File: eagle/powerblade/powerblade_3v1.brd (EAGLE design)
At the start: 27.9 x 27.9 mm, 91 parts, among them J1 JTAG_14PIN_IDC, J21 AC_INTBFILM, J4 TC2030-JLINK-NL, Q1 2N7002, Q3 2SK1829, Q4 2SK1829, U1 TPS62122, U2 MCP6V3, U3 MSP430FR5738, U4 NRF51822QF, U6 MAX9910, U7 OPA2369, X1 16MHz, X2 ABS05-32.768KHZ-9-T, X3 32.768kHz

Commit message: finished parts
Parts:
- R11, R22: value 134k 1% -> 670k
- R12, R13: value 67k 1% -> 330k
- R15: value NP -> 1M 1%
- R16: value 0 -> 75 1%
- R18: value 2.49 1% -> 4.99 1%
- R35: value 2k 1% -> 20k
- R37: value 90k 1% -> 887k 1%
- R38: value 3.1k 1% -> 137k 1%
- R39: value 100k 1% -> 71.5k 1%
- R40: value 100k 1% -> 1M 1%
- R6: value 220k -> 660k
- RF: value 1.5k 1% -> 4.99k 1%
- RI1, RI2: value 220k 1% -> 953k 1%
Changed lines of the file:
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@@
 <attribute name="NAME" x="5.23875" y="-0.762" size="0.762" layer="25" rot="R90"/>
 </element>
-<element name="R15" library="rcl" package="R0402" value="NP" x="3.65125" y="-1.27" smashed="yes">
-<attribute name="DIGIKEY" value="NP" x="3.65125" y="22.86" size="1.778" layer="27" display="off"/>
+<element name="R15" library="rcl" package="R0402" value="1M 1%" x="3.65125" y="-1.27" smashed="yes">
 <attribute name="VALUE" x="2.06375" y="-3.81" size="0.762" layer="27"/>
 </element>
-<element name="R16" library="rcl" package="R0402" value="0" x="3.65125" y="-2.44475" smashed="yes">
-<attribute name="DIGIKEY" value="P0.0JCT-ND" x="-1.42875" y="16.60525" size="1.778" layer="27" display="off"/>
+<element name="R16" library="rcl" package="R0402" value="75 1%" x="3.65125" y="-2.44475" smashed="yes">
 <attribute name="NAME" x="1.42875" y="-4.66725" size="0.762" layer="25"/>
 </element>
@@
 <attribute name="NAME" x="0.4445" y="4.12115" size="0.762" layer="25"/>
 </element>
-<element name="R18" library="rcl" package="R0402" value="2.49 1%" x="3.4925" y="4.28625" smashed="yes" rot="R180">
+<element name="R18" library="rcl" package="R0402" value="4.99 1%" x="3.4925" y="4.28625" smashed="yes" rot="R180">
 <attribute name="DIGIKEY" value="541-2.49LLCT-ND" x="3.4925" y="14.44625" size="1.778" layer="27" rot="R180" display="off"/>
 <attribute name="NAME" x="4.445" y="3.81" size="0.762" layer="25" rot="R180"/>
@@
 <attribute name="NAME" x="-11.39825" y="1.17475" size="0.762" layer="25" rot="R180"/>
 </element>
-<element name="RF" library="rcl" package="R0402" value="1.5k 1%" x="-12.16025" y="7.46125" smashed="yes" rot="R180">
-<attribute name="DIGIKEY" value="P1.50KLCT-ND" x="-4.54025" y="36.67125" size="1.778" layer="27" rot="R180" display="off"/>
+<element name="RF" library="rcl" package="R0402" value="4.99k 1%" x="-12.16025" y="7.46125" smashed="yes" rot="R180">
 <attribute name="NAME" x="-10.8585" y="6.19125" size="0.762" layer="25"/>
 </element>
 <element name="R20" library="rcl" package="R0402" value="1M 1%" x="-12.2555" y="3.14325" smashed="yes" rot="R180">
-<attribute name="DIGIKEY" value="P10.0KLCT-ND" x="10.6045" y="37.43325" size="1.778" layer="27" rot="R180" display="off"/>
 <attribute name="NAME" x="-11.46175" y="0.28575" size="0.762" layer="25" rot="R180"/>
 </element>
 <element name="R21" library="rcl" package="R0402" value="1M 1%" x="-9.11225" y="6.9215" smashed="yes" rot="R270">
-<attribute name="DIGIKEY" value="P10.0KLCT-ND" x="-43.40225" y="6.9215" size="1.778" layer="27" rot="R270" display="off"/>
 <attribute name="NAME" x="-8.47725" y="7.5565" size="0.762" layer="25" rot="R270"/>
 </element>
-<element name="RI1" library="rcl" package="R0402" value="220k 1%" x="-11.58875" y="9.2075" smashed="yes" rot="R270">
-<attribute name="DIGIKEY" value="P220KLCT-ND" x="-61.11875" y="9.2075" size="1.778" layer="27" rot="R270" display="off"/>
+<element name="RI1" library="rcl" package="R0402" value="953k 1%" x="-11.58875" y="9.2075" smashed="yes" rot="R270">
 <attribute name="NAME" x="-10.95375" y="10.63625" size="0.762" layer="25" rot="R270"/>
 </element>
-<element name="RI2" library="rcl" package="R0402" value="220k 1%" x="-9.7155" y="8.5725" smashed="yes" rot="R180">
-<attribute name="DIGIKEY" value="P220KLCT-ND" x="-0.8255" y="63.1825" size="1.778" layer="27" rot="R180" display="off"/>
+<element name="RI2" library="rcl" package="R0402" value="953k 1%" x="-9.7155" y="8.5725" smashed="yes" rot="R180">
 <attribute name="NAME" x="-8.128" y="9.8425" size="0.762" layer="25" rot="R180"/>
 </element>
@@
 <attribute name="NAME" x="-5.36575" y="-5.68325" size="0.762" layer="25" rot="R90"/>
 </element>
-<element name="R35" library="rcl" package="R0402" value="2k 1%" x="-0.635" y="-1.23825" smashed="yes" rot="R90">
+<element name="R35" library="rcl" package="R0402" value="20k" x="-0.635" y="-1.23825" smashed="yes" rot="R90">
 <attribute name="DIGIKEY" value="P2.00KLCT-ND" x="71.755" y="-16.47825" size="1.778" layer="27" rot="R90" display="off"/>
 <attribute name="NAME" x="0.3175" y="-4.572" size="0.762" layer="25" rot="R90"/>
 </element>
-<element name="R37" library="rcl" package="R0402" value="90k 1%" x="-2.8575" y="1.905" smashed="yes" rot="R180">
+<element name="R37" library="rcl" package="R0402" value="887k 1%" x="-2.8575" y="1.905" smashed="yes" rot="R180">
 <attribute name="DIGIKEY" value="P90.9KLCT-ND" x="4.7625" y="79.375" size="1.778" layer="27" rot="R180" display="off"/>
 <attribute name="NAME" x="-1.905" y="1.42875" size="0.762" layer="25" rot="R180"/>
 </element>
-<element name="R38" library="rcl" package="R0402" value="3.1k 1%" x="-2.8575" y="3.048" smashed="yes">
+<element name="R38" library="rcl" package="R0402" value="137k 1%" x="-2.8575" y="3.048" smashed="yes">
 <attribute name="DIGIKEY" value="P3.09KHCT-ND" x="-19.3675" y="-89.662" size="1.778" layer="27" display="off"/>
 <attribute name="NAME" x="-1.27" y="4.318" size="0.762" layer="25"/>
 </element>
-<element name="R40" library="rcl" package="R0402" value="100k 1%" x="-3.96875" y="-2.9845" smashed="yes" rot="R180">
-<attribute name="DIGIKEY" value="P100KLCT-ND" x="11.27125" y="101.1555" size="1.778" layer="27" rot="R180" display="off"/>
+<element name="R40" library="rcl" package="R0402" value="1M 1%" x="-3.96875" y="-2.9845" smashed="yes" rot="R180">
 <attribute name="NAME" x="-3.175" y="-3.77825" size="0.762" layer="25" rot="R180"/>
 </element>
@@
 <attribute name="DIGIKEY" value="5126K-ND" x="158.4325" y="-32.766" size="1.778" layer="27" rot="R90" display="off"/>
 </element>
-<element name="R39" library="rcl" package="R0402" value="100k 1%" x="-1.55575" y="-2.9845" smashed="yes" rot="R180">
+<element name="R39" library="rcl" package="R0402" value="71.5k 1%" x="-1.55575" y="-2.9845" smashed="yes" rot="R180">
 <attribute name="DIGIKEY" value="P100KLCT-ND" x="-1.55575" y="-2.9845" size="1.778" layer="27" rot="R180" display="off"/>
 <attribute name="NAME" x="-0.60325" y="-4.572" size="0.762" layer="25" rot="R180"/>
@@
 <attribute name="DIGIKEY" value="NP" x="-7.62" y="-80.772" size="1.778" layer="27" display="off"/>
 </element>
-<element name="R11" library="rcl" package="R0603" value="134k 1%" x="-6.858" y="-65.532">
-<attribute name="DIGIKEY" value="P133KHCT-ND" x="-15.24" y="-130.302" size="1.778" layer="27" display="off"/>
-</element>
-<element name="R12" library="rcl" package="R0603" value="67k 1%" x="1.524" y="-65.532">
-<attribute name="DIGIKEY" value="P66.5KHCT-ND" x="-15.24" y="-135.636" size="1.778" layer="27" display="off"/>
-</element>
+<element name="R11" library="rcl" package="R0603" value="670k" x="-6.858" y="-65.532"/>
+<element name="R12" library="rcl" package="R0603" value="330k" x="1.524" y="-65.532"/>
 <element name="X3" library="general" package="0805" value="32.768kHz" x="6.858" y="-48.768">
 <attribute name="DIGIKEY" value="535-12373-1-ND" x="-15.24" y="-141.732" size="1.778" layer="27" display="off"/>
@@
 <attribute name="DIGIKEY" value="2SK1829TE85LFCT-ND" x="-12.192" y="-125.73" size="1.778" layer="27" display="off"/>
 </element>
-<element name="R6" library="rcl" package="R0603" value="220k" x="-12.192" y="-129.54"/>
+<element name="R6" library="rcl" package="R0603" value="660k" x="-12.192" y="-129.54"/>
 <element name="R10" library="rcl" package="R0603" value="220k" x="-12.192" y="-134.874"/>
-<element name="R13" library="rcl" package="R0603" value="67k 1%" x="-12.192" y="-140.208">
-<attribute name="DIGIKEY" value="P66.5KHCT-ND" x="-12.192" y="-140.208" size="1.778" layer="27" display="off"/>
-</element>
-<element name="R22" library="rcl" package="R0603" value="134k 1%" x="-12.192" y="-145.542">
-<attribute name="DIGIKEY" value="P133KHCT-ND" x="-12.192" y="-145.542" size="1.778" layer="27" display="off"/>
-</element>
+<element name="R13" library="rcl" package="R0603" value="330k" x="-12.192" y="-140.208"/>
+<element name="R22" library="rcl" package="R0603" value="670k" x="-12.192" y="-145.542"/>
 </elements>
 <signals>

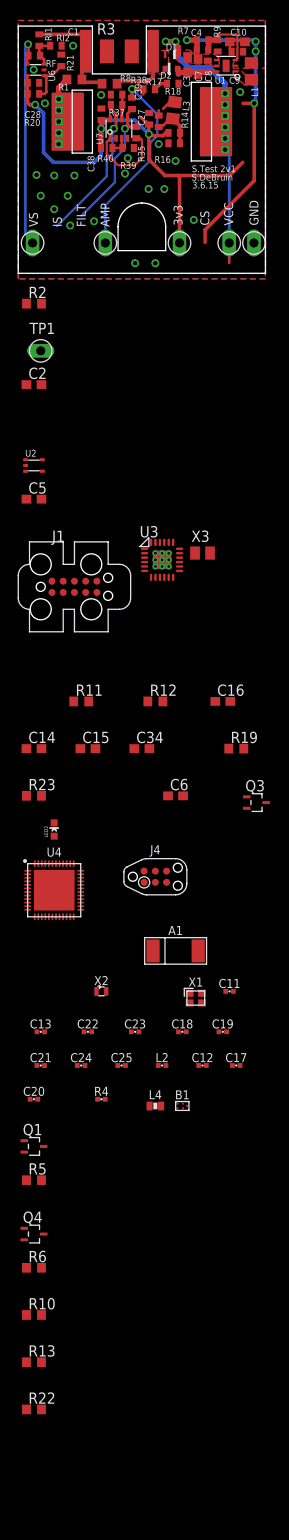
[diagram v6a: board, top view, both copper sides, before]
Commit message: post mortem changes to schematic
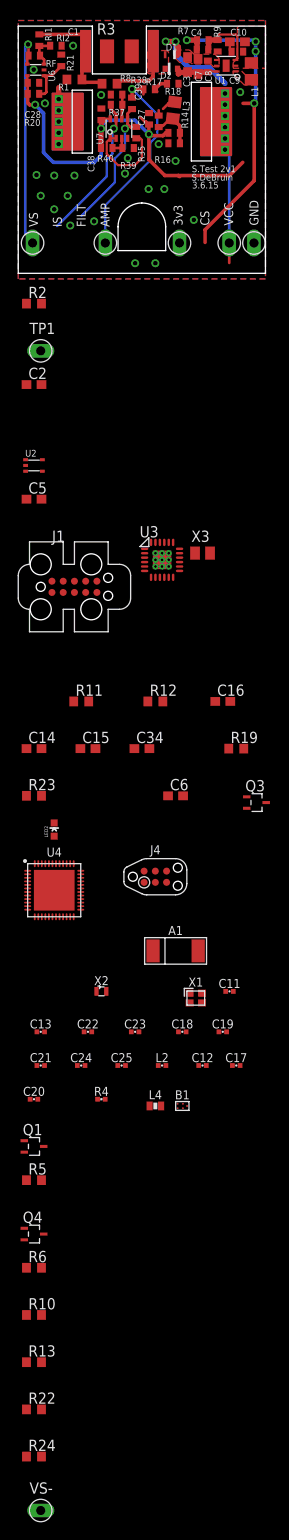
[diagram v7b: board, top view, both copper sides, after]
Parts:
- added R24: 1 1%, rcl:R0603
- added VS-: TP_LONG, skyspecs:TP_LONG
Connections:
- new net N$12: J21.P, J21.P1, J21.P2, J21.P3, J21.P4, J21.P5, J21.P6, R1.1
- new net N$7: C10.1, C4.1, C9.1, L1.1, R24.1, R7.2, U1.P2, VS+.P$1
- new net PWM_CURRENT: U3.P3
- new net PWM_VOLTAGE: U3.P4
- net +3V3: now also R24.2, VS-.P$1; no longer C10.1, C4.1, C9.1, L1.1, R7.2, U1.P2, VS+.P$1
- net GND: now also D1.A, J21.N, J21.N1, J21.N2, J21.N3, J21.N4, J21.N5; no longer D2.A
- net N$2: now also C1.1, D1.C, D2.A, R3.2, R8.2; no longer J21.N, J21.N1, J21.N2, J21.N3, J21.N4, J21.N5, R1.1
- net N$8: now also U3.P1; no longer U3.P3
- net VCC: now also D2.C; no longer D1.C, J21.P, J21.P1, J21.P2, J21.P3, J21.P4, J21.P5, J21.P6
- net VCC_SENSE: now also U3.P2; no longer U3.P4
- net ZC: no longer C1.1, D1.A, D2.C, R3.2, R8.2
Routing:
- net +3V3: track 94.8 -> 50.8 mm, vias 7 -> 3
- net N$7: track 0.00 -> 36.4 mm, vias 0 -> 4
- net VCC: track 34.2 -> 12.3 mm, vias 2 -> 0
- net N$2: track 9.01 -> 19.6 mm, vias 0 -> 2
- net GND: track 6.25 -> 13.8 mm
- net ZC: track 7.29 -> 0.00 mm

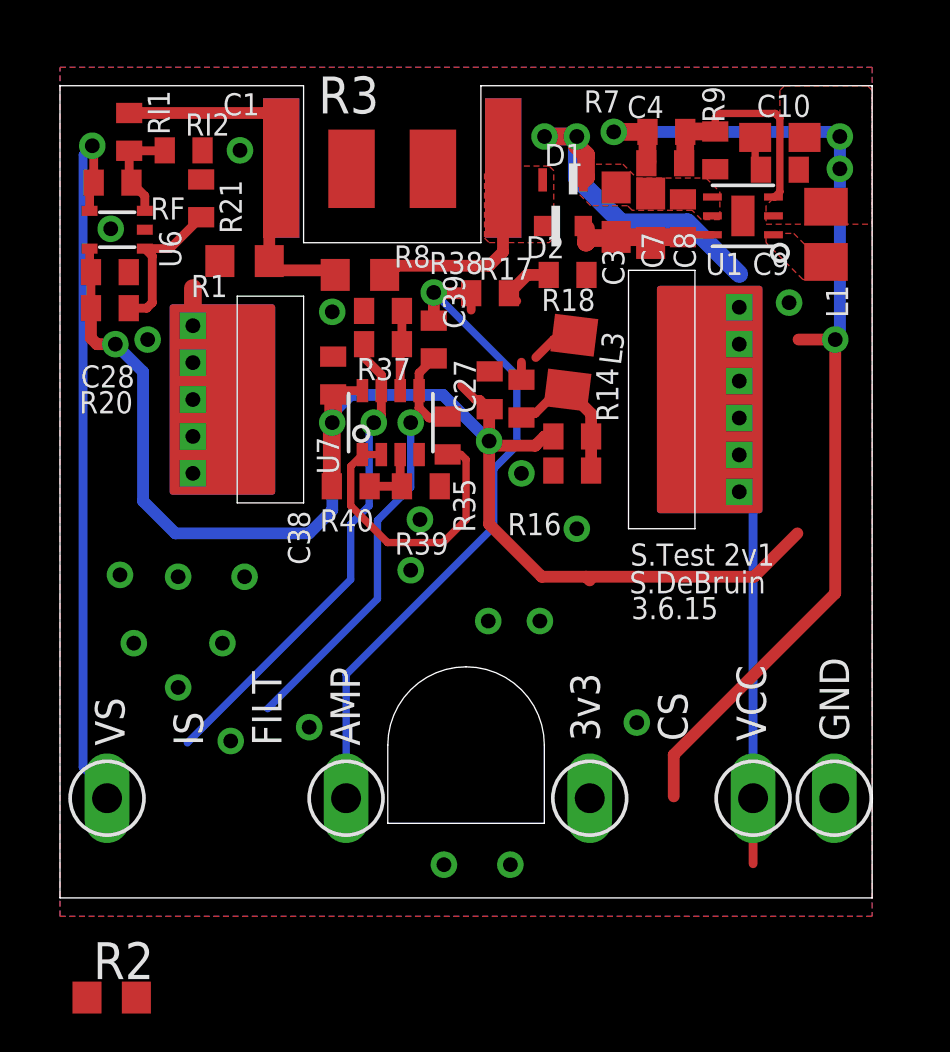
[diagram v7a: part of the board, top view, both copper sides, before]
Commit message: updated powerblade schematic
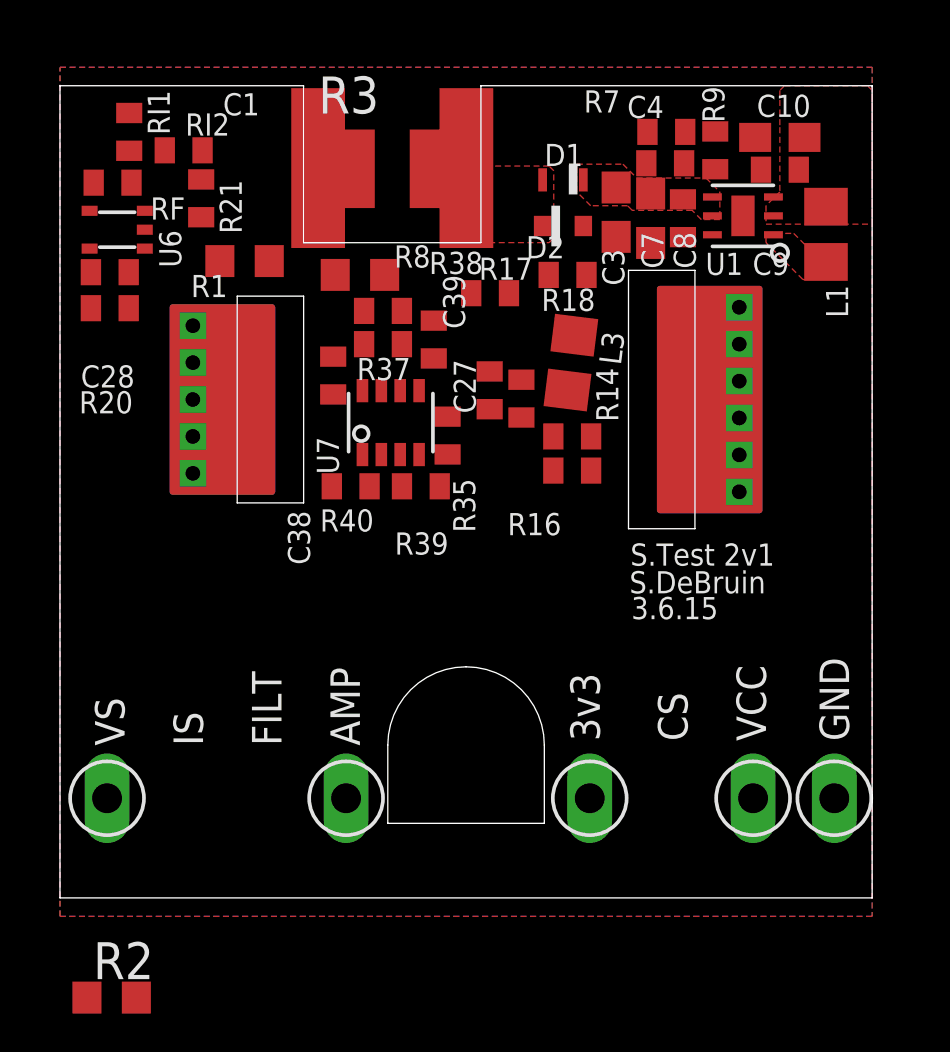
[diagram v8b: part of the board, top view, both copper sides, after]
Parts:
- C1: device rcl:C2220-EDGE -> rcl:C2220K
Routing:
- net +3V3: track 50.8 -> 0.00 mm, vias 3 -> 0
- net N$7: track 36.4 -> 0.00 mm, vias 4 -> 0
- net V_SENSE: track 25.2 -> 0.00 mm, vias 1 -> 0
- net N$61: track 23.8 -> 0.00 mm, vias 1 -> 0
- net N$2: track 19.6 -> 0.00 mm, vias 2 -> 0
- net N$1: track 16.7 -> 0.00 mm, vias 1 -> 0
- net N$67: track 15.6 -> 0.00 mm, vias 1 -> 0
- net GND: track 13.8 -> 0.00 mm, vias 22 -> 0
- net VTEST: track 13.0 -> 0.00 mm
- net VCC: track 12.3 -> 0.00 mm
- net N$68: track 10.2 -> 0.00 mm
- net N$13: track 7.78 -> 0.00 mm
- net N$40: track 5.24 -> 0.00 mm
- net N$37: track 5.08 -> 0.00 mm
- net N$41: track 3.52 -> 0.00 mm
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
